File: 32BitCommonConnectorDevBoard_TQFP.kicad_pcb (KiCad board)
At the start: 2 copper layers, 70.6 x 84.3 mm, 26 parts, among them J1 Conn_01x06, J2 Conn_02x32_Counter_Clockwise, J3 AVR-ISP-6, SW1 SW_Push, U1 LD1117V33, U2 ATmega1281-16A, Y1 Crystal

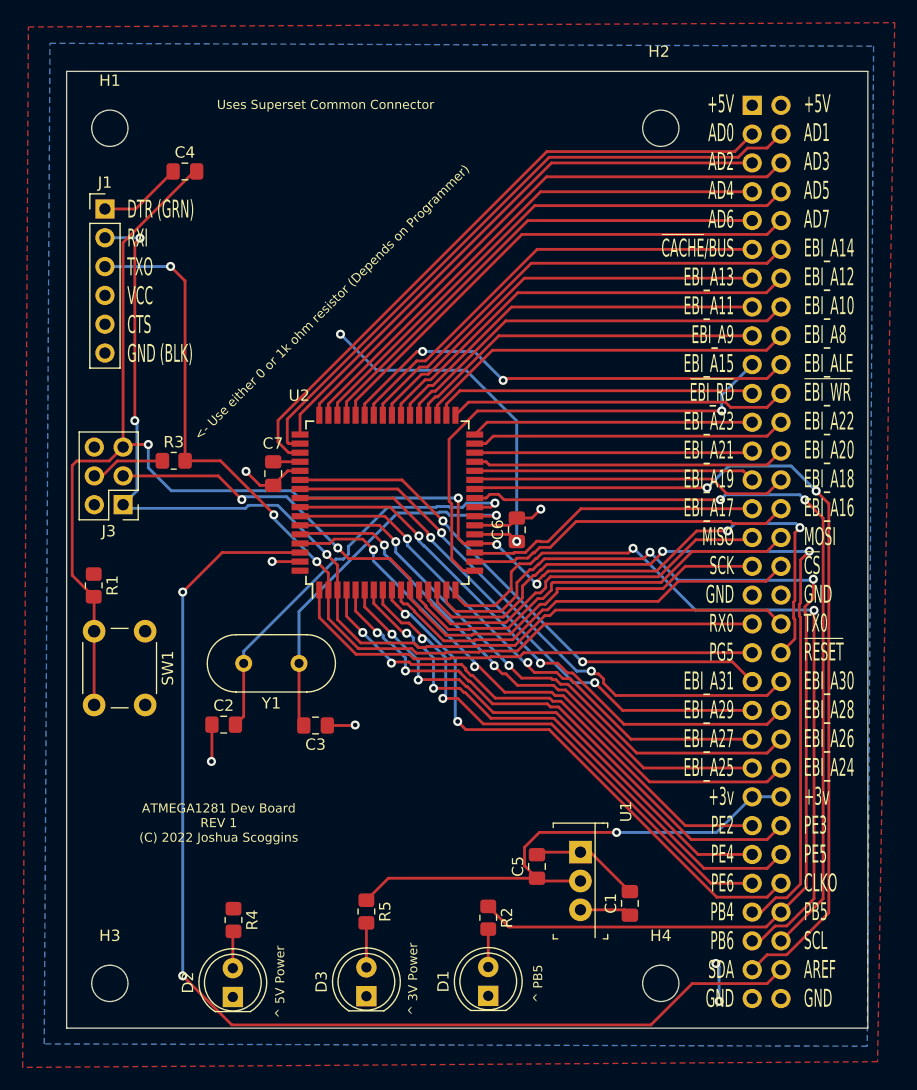
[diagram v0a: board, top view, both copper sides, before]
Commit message: Clean up layouts and shrink board slightly
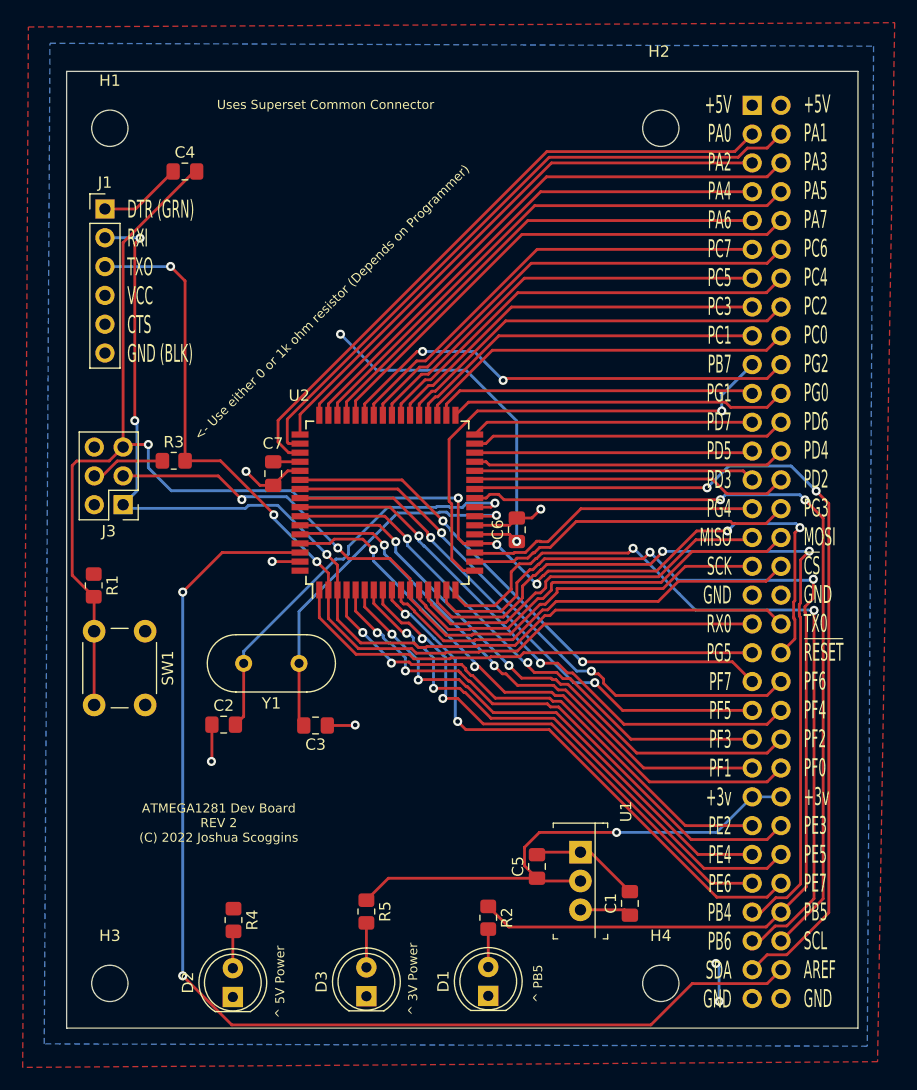
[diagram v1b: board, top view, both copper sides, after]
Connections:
- net /CLKO renamed /PE7
- net /EBI_A10 renamed /PC2
- net /EBI_A11 renamed /PC3
- net /EBI_A12 renamed /PC4
- net /EBI_A13 renamed /PC5
- net /EBI_A14 renamed /PC6
- net /EBI_A15 renamed /PB7
- net /EBI_A16 renamed /PG3
- net /EBI_A17 renamed /PG4
- net /EBI_A18 renamed /PD2
- net /EBI_A19 renamed /PD3
- net /EBI_A20 renamed /PD4
- net /EBI_A21 renamed /PD5
- net /EBI_A22 renamed /PD6
- net /EBI_A23 renamed /PD7
- net /EBI_A24 renamed /PF0
- net /EBI_A25 renamed /PF1
- net /EBI_A26 renamed /PF2
- net /EBI_A27 renamed /PF3
- net /EBI_A28 renamed /PF4
- net /EBI_A29 renamed /PF5
- net /EBI_A30 renamed /PF6
- net /EBI_A31 renamed /PF7
- net /EBI_A8 renamed /PC0
- net /EBI_A9 renamed /PC1
- net /EBI_AD0 renamed /PA0
- net /EBI_AD1 renamed /PA1
- net /EBI_AD2 renamed /PA2
- net /EBI_AD3 renamed /PA3
- net /EBI_AD4 renamed /PA4
- net /EBI_AD5 renamed /PA5
- net /EBI_AD6 renamed /PA6
- net /EBI_AD7 renamed /PA7
- net /EBI_ALE renamed /PG2
- net /~{CACHE}/BUS renamed /PC7
- net /~{EBI_RD} renamed /PG1
- net /~{EBI_WR} renamed /PG0
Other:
- board size 70.6 x 84.3 mm -> 69.8 x 84.3 mm
- board text added: "+5V PA0 PA2 PA4 PA6 PC7 PC5 PC3 PC1 PB7 PG1 PD7 PD5 PD3 PG4 MISO SCK GND RX0 PG5 PF7 PF5 PF3 PF1 +3v PE2 PE4 PE6 PB4 PB6 SDA GND"
- board text added: "+5V PA1 PA3 PA5 PA7 PC6 PC4 PC2 PC0 PG2 PG0 PD6 PD4 PD2 PG3 MOSI ~{CS} GND TX0 ~{RESET} PF6 PF4 PF2 PF0 +3v PE3 PE5 PE7 PB5 SCL AREF GND"
- board text added: "ATMEGA1281 Dev Board REV 2 (C) 2022 Joshua Scoggins"
- board text removed: "+5V AD0 AD2 AD4 AD6 ~{CACHE}/BUS EBI_A13 EBI_A11 EBI_A9 EBI_A15 ~{EBI_RD} EBI_A23 EBI_A21 EBI_A19 EBI_A17 MISO SCK GND RX0 PG5 EBI_A31 EBI_A29 EBI_A27 EBI_A25 +3v PE2 PE4 PE6 PB4 PB6 SDA GND"
- board text removed: "+5V AD1 AD3 AD5 AD7 EBI_A14 EBI_A12 EBI_A10 EBI_A8 EBI_ALE ~{EBI_WR} EBI_A22 EBI_A20 EBI_A18 EBI_A16 MOSI ~{CS} GND TX0 ~{RESET} EBI_A30 EBI_A28 EBI_A26 EBI_A24 +3v PE3 PE5 CLKO PB5 SCL AREF GND"
- board text removed: "ATMEGA1281 Dev Board REV 1 (C) 2022 Joshua Scoggins"

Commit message: Update revision number and put share alike logo back in
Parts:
- added REF**: CreativeCommonShareAlikeCopperSmall, CreativeCommon:CreativeCommonShareAlikeCopperSmall, F.Cu at (130.4, 61.9)
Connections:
- J2 pad 19: /PB7 -> /PG5
- J2 pad 39: /PG5 -> /PE7
- J2 pad 56: /PE7 -> /PB4
- J2 pad 57: /PB4 -> /PB5
- J2 pad 58: /PB5 -> /PB6
- J2 pad 59: /PB6 -> /PB7
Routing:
- net /PB7: track 43.4 -> 66.4 mm, vias 1 -> 2
- net /PB4: track 72.5 -> 57.5 mm, vias 2 -> 4
- net /PE7: track 49.7 -> 35.1 mm
- net /PG5: track 42.3 -> 49.2 mm, vias 0 -> 5
- net /PB6: track 70.1 -> 65.7 mm
- net /PF5: track 47.9 -> 49.7 mm
- net /RX0: track 84.1 -> 85.9 mm
- net /PF6: track 50.8 -> 52.0 mm
- net /~{RESET}: track 136.6 -> 135.5 mm
- net /PF4: track 51.1 -> 52.0 mm
- net /PF7: track 47.4 -> 48.1 mm
- net /TX0: track 95.5 -> 96.2 mm, vias 3 -> 5
- net /~{CS}: track 38.7 -> 39.2 mm
- net /PF0: track 52.8 -> 53.3 mm
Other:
- board text added: "+5V PA0 PA2 PA4 PA6 PC7 PC5 PC3 PC1 PG5 PG1 PD7 PD5 PD3 PG4 MISO SCK GND RX0 PE7 PF7 PF5 PF3 PF1 +3v PE2 PE4 PE6 PB5 PB7 SDA GND"
- board text added: "+5V PA1 PA3 PA5 PA7 PC6 PC4 PC2 PC0 PG2 PG0 PD6 PD4 PD2 PG3 MOSI ~{CS} GND TX0 ~{RESET} PF6 PF4 PF2 PF0 +3v PE3 PE5 PB4 PB6 SCL AREF GND"
- board text added: "ATMEGA1281 Dev Board REV 3 (C) 2022 Joshua Scoggins"
- board text removed: "+5V PA0 PA2 PA4 PA6 PC7 PC5 PC3 PC1 PB7 PG1 PD7 PD5 PD3 PG4 MISO SCK GND RX0 PG5 PF7 PF5 PF3 PF1 +3v PE2 PE4 PE6 PB4 PB6 SDA GND"
- board text removed: "+5V PA1 PA3 PA5 PA7 PC6 PC4 PC2 PC0 PG2 PG0 PD6 PD4 PD2 PG3 MOSI ~{CS} GND TX0 ~{RESET} PF6 PF4 PF2 PF0 +3v PE3 PE5 PE7 PB5 SCL AREF GND"
- board text removed: "ATMEGA1281 Dev Board REV 2 (C) 2022 Joshua Scoggins"
